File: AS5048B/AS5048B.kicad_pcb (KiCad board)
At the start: 2 copper layers, 23.2 x 23.2 mm, 6 parts, among them Q1 AS5048B-HTSP-500

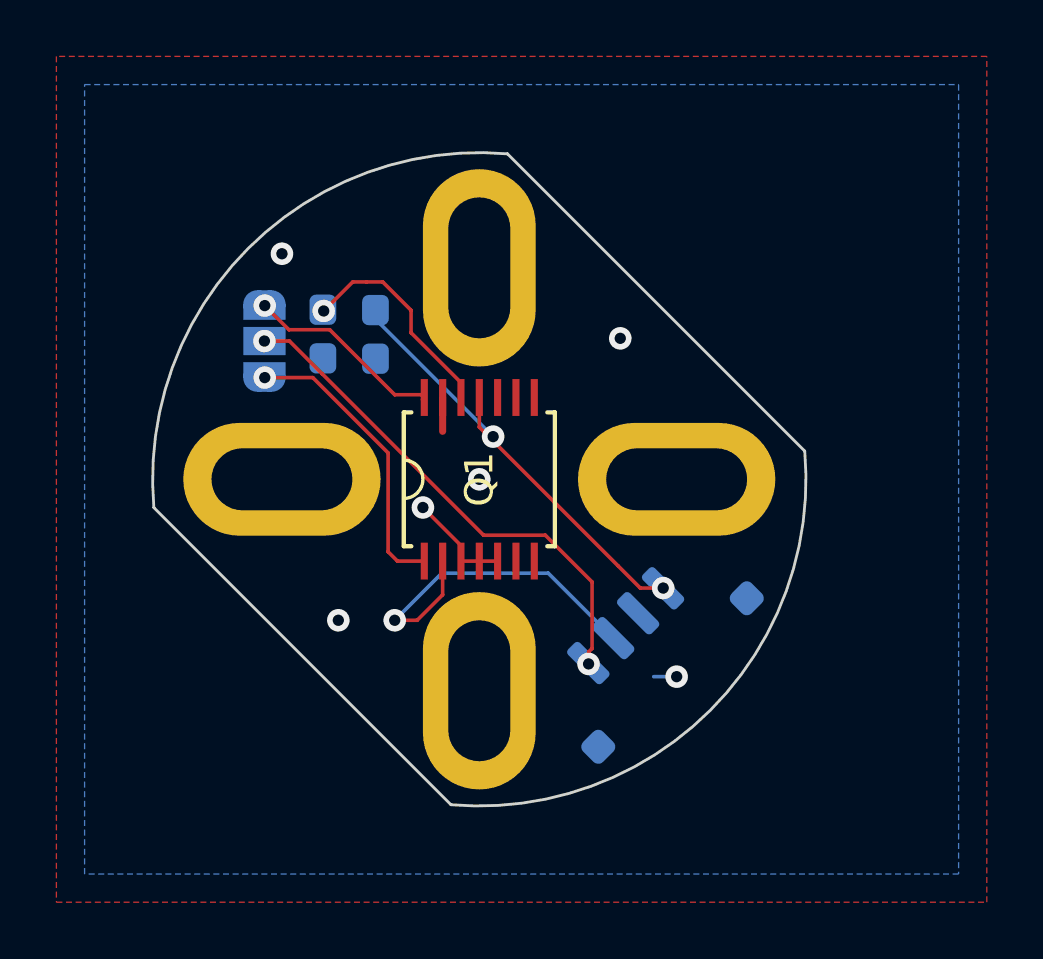
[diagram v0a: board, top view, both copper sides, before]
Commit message: Added Text
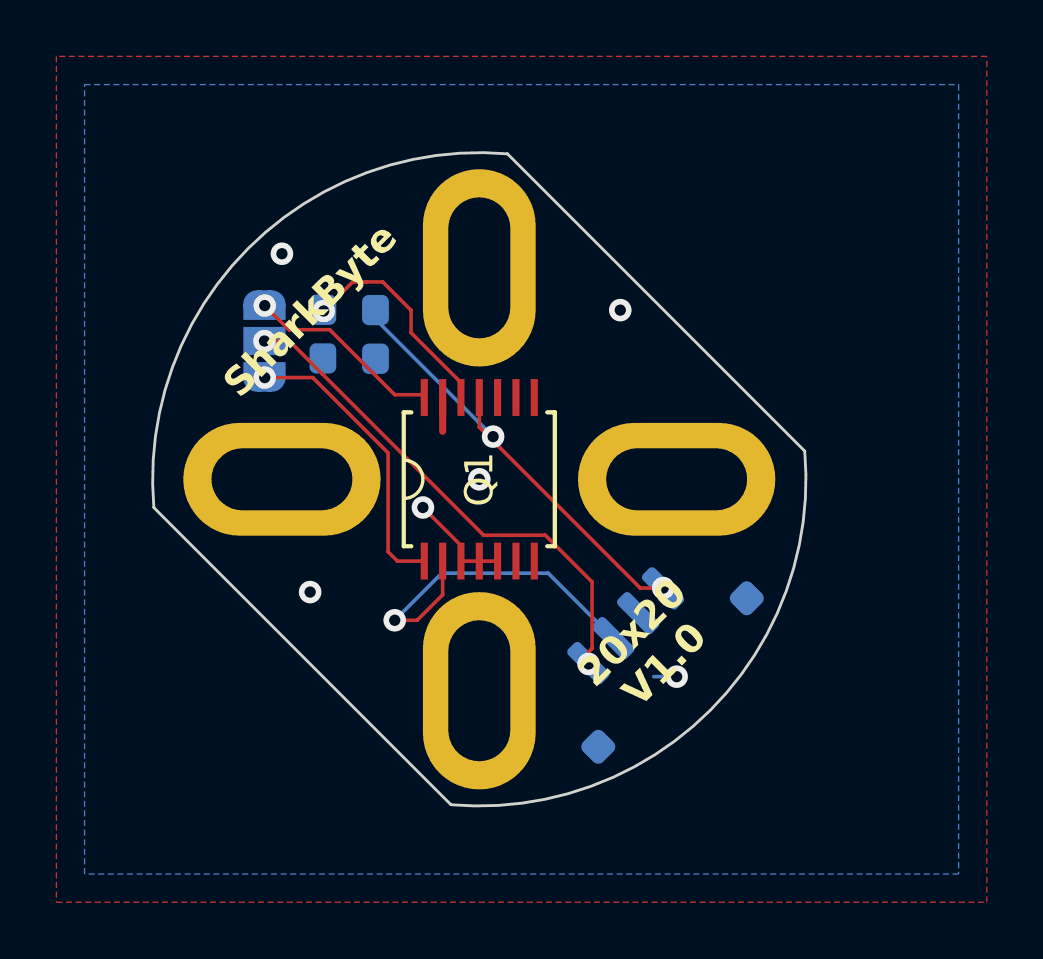
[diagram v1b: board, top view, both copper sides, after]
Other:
- board text added: "20x20 V1.0"
- board text added: "SharkByte"

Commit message: Update AS5048B.kicad_pcb
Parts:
- added G***: LOGO, Sharkbite:Logo1 8x8, F.Cu at (143.2, 143.6)
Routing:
- net Net-(Q1-VDD3V): track 7.77 -> 12.7 mm
- net /PWM: track 7.11 -> 9.89 mm
- net Net-(J1-Pin_4): track 18.3 -> 21.1 mm
- net GND: vias 6 -> 7

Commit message: Updated Logo
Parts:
- C1, C2: footprint Capacitor_SMD:C_0603_1608Metric_Pad1.08x0.95mm_HandSolder -> Capacitor_SMD:C_0603_1608Metric
- G***: moved to B.Cu
- moved JP1 12.8 mm to (155.2, 144.8), turned to 135 degrees
- moved G*** 10.0 mm to (151.0, 150.0)
- moved C1 1.22 mm to (143.2, 144.8)
- moved C2 1.22 mm to (145.1, 144.9)
- moved Je 0.71 mm to (156.0, 156.0)
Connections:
- Je pad MP: (no net) -> GND
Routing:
- net GND: track 5.78 -> 15.7 mm
- net /PWM: track 9.89 -> 15.0 mm
- net +5V: track 16.3 -> 20.2 mm
- net Net-(J1-Pin_3): track 12.7 -> 9.25 mm
- net Net-(J1-Pin_4): track 21.1 -> 18.5 mm
- net /I2C: track 10.4 -> 12.1 mm
- net Net-(Q1-VDD3V): track 12.7 -> 11.4 mm
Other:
- board text added: "PWM"
